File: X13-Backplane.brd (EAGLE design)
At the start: 86.4 x 139.3 mm, 36 parts, among them J1 PXC-PTSM-04-RA-1778641, J2 PXC-PTSM-04-RA-1778641, J3 PXC-8-RA-1778683, J4 PXC-PTSM-04-RA-1778641, J5 PXC-PTSM-04-RA-1778641, J6 284512-4, J8 PXC-8-RA-1778683

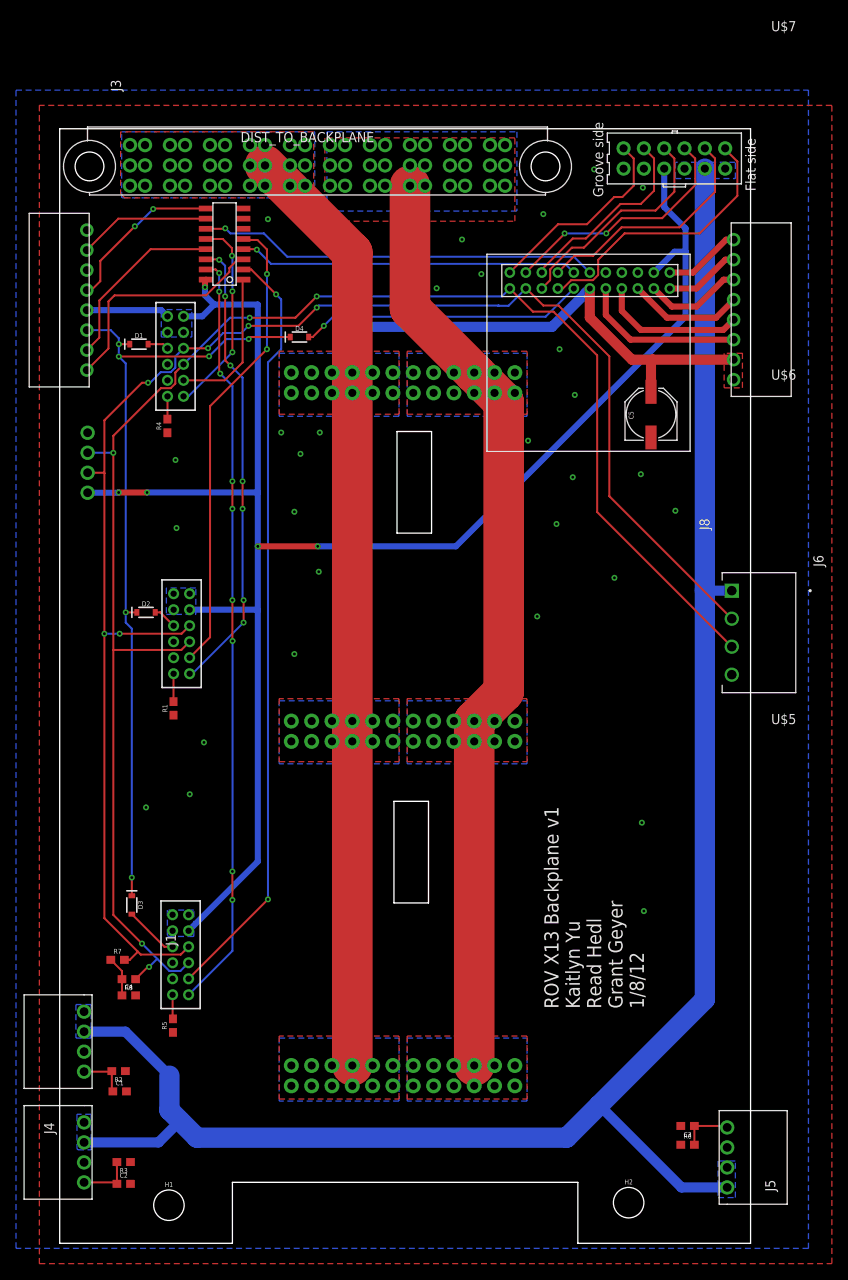
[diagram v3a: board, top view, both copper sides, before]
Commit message: Added third cutout and models for te 4 pin conn
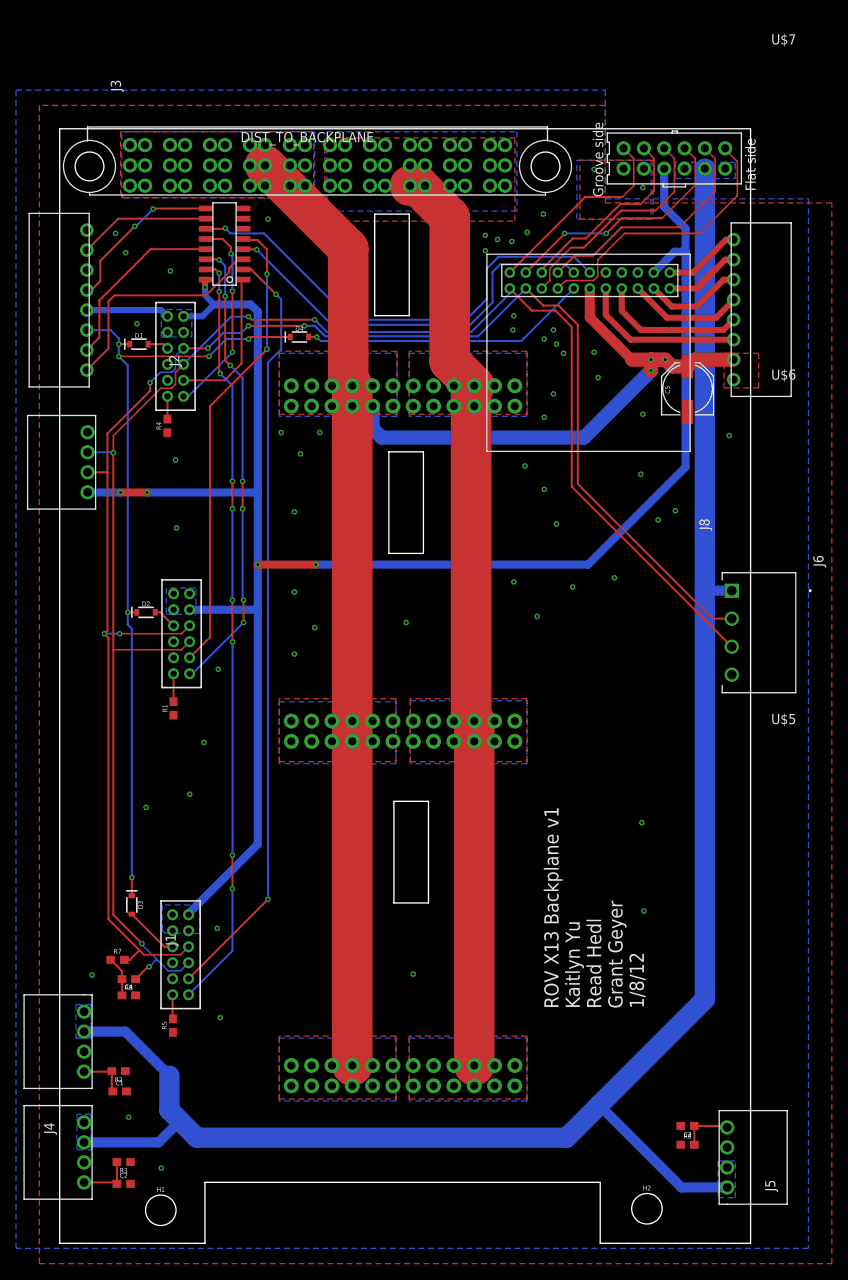
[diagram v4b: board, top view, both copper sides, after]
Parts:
- J6: value 284512-4 -> (none); device 284512-4:TE_284512-4 -> te 3.5m mm horiz 4 pin:TE_284512-4
- moved J2 7.56 mm to (11.1, 101.4), flipped to the top, turned to 270 degrees
- moved C5 5.57 mm to (86.1, 106.8)
- moved H2 2.41 mm to (81.0, 4.32)
- moved U$7 1.65 mm to (101.6, 143.5)
- moved H1 1.20 mm to (20.3, 4.13)
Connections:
- net 3.3V: now also J2.4; no longer J2.1
- net CAN_H: now also J2.3; no longer J2.2
- net CAN_L: now also J2.2; no longer J2.3
- net GND: now also J2.1; no longer J2.4
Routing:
- net 3.3V: track 225.7 -> 235.1 mm
- net SWCLK_4: track 50.3 -> 59.1 mm
- net SWDIO_4: track 42.5 -> 51.1 mm
- net 12V: track 181.8 -> 187.6 mm, vias 0 -> 3
- net CAN_H: track 203.8 -> 206.2 mm
- net CAN_L: track 205.3 -> 207.6 mm
- net 12VGND: track 116.4 -> 114.2 mm
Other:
- outline, holes or cut-outs redrawn

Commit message: add tStop polygon
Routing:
- net 12V: track 187.6 -> 209.1 mm
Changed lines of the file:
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@@
 <layer number="27" name="tValues" color="7" fill="1" visible="yes" active="yes"/>
 <layer number="28" name="bValues" color="7" fill="1" visible="yes" active="yes"/>
-<layer number="29" name="tStop" color="7" fill="3" visible="no" active="yes"/>
+<layer number="29" name="tStop" color="7" fill="3" visible="yes" active="yes"/>
 <layer number="30" name="bStop" color="7" fill="6" visible="no" active="yes"/>
 <layer number="31" name="tCream" color="7" fill="4" visible="no" active="yes"/>
@@
 <wire x1="51.308" y1="128.651" x2="51.308" y2="115.951" width="0" layer="20"/>
 <wire x1="51.308" y1="115.951" x2="46.99" y2="115.951" width="0" layer="20"/>
+<polygon width="0.1524" layer="29">
+<vertex x="41.529" y="17.526"/>
+<vertex x="46.736" y="17.526"/>
+<vertex x="46.736" y="112.014"/>
+<vertex x="46.355" y="112.014"/>
+<vertex x="46.355" y="125.222"/>
+<vertex x="41.148" y="130.429"/>
+<vertex x="33.655" y="130.429"/>
+<vertex x="40.64" y="123.444"/>
+<vertex x="40.64" y="103.632"/>
+<vertex x="41.529" y="102.743"/>
+</polygon>
+<polygon width="0.1524" layer="29">
+<vertex x="42.164" y="130.175"/>
+<vertex x="65.024" y="130.175"/>
+<vertex x="65.024" y="129.032"/>
+<vertex x="63.246" y="127.254"/>
+<vertex x="58.928" y="127.254"/>
+<vertex x="58.928" y="111.76"/>
+<vertex x="62.357" y="108.331"/>
+<vertex x="62.357" y="103.759"/>
+<vertex x="61.722" y="103.124"/>
+<vertex x="61.722" y="63.246"/>
+<vertex x="62.103" y="62.865"/>
+<vertex x="62.103" y="17.272"/>
+<vertex x="56.769" y="17.272"/>
+<vertex x="56.769" y="68.453"/>
+<vertex x="56.388" y="68.834"/>
+<vertex x="56.388" y="103.251"/>
+<vertex x="53.594" y="106.045"/>
+<vertex x="53.594" y="127.127"/>
+<vertex x="53.467" y="127.254"/>
+<vertex x="45.085" y="127.254"/>
+</polygon>
 </plain>
 <attributes>
@@
 <via x="70.612" y="111.252" extent="1-16" drill="0.35"/>
 <via x="74.93" y="108.204" extent="1-16" drill="0.35"/>
-<via x="74.422" y="111.379" extent="1-16" drill="0.35"/>
+<via x="75.438" y="110.236" extent="1-16" drill="0.35"/>
 <via x="68.199" y="103.251" extent="1-16" drill="0.35"/>
-<via x="80.518" y="103.632" extent="1-16" drill="0.35"/>
+<via x="81.534" y="102.235" extent="1-16" drill="0.35"/>
 <via x="91.313" y="100.965" extent="1-16" drill="0.35"/>
 <via x="16.256" y="15.748" extent="1-16" drill="0.35"/>
@@
 </polygon>
 <contactref element="J2" pad="1"/>
+<via x="39.37" y="72.263" extent="1-16" drill="0.35"/>
+<via x="30.607" y="58.42" extent="1-16" drill="0.35"/>
+<wire x1="30.57525" y1="126.8095" x2="21.463" y2="121.539" width="0" layer="19" extent="1-1"/>
 </signal>
 <signal name="SWDIO_3">
@@
 <wire x1="35.306" y1="117.983" x2="35.306" y2="111.76" width="0.254" layer="16"/>
 <wire x1="31.5595" y1="121.7295" x2="34.671" y2="118.618" width="0.254" layer="1"/>
-<wire x1="33.655" y1="42.99" x2="23.733" y2="33.068" width="0.254" layer="1"/>
+<wire x1="23.733" y1="33.068" x2="33.655" y2="42.99" width="0.254" layer="1"/>
 <wire x1="35.306" y1="111.76" x2="33.655" y2="110.109" width="0.254" layer="16"/>
 <wire x1="33.655" y1="110.109" x2="33.655" y2="42.99" width="0.254" layer="16"/>
@@
 <wire x1="29.21" y1="91.821" x2="29.21" y2="80.391" width="0.254" layer="16"/>
 <via x="29.21" y="80.391" extent="1-16" drill="0.35"/>
-<wire x1="29.21" y1="80.391" x2="29.21" y2="75.184" width="0.254" layer="1"/>
-<wire x1="29.21" y1="75.184" x2="29.23049375" y2="75.16350625" width="0.254" layer="1"/>
-<via x="29.23049375" y="75.16350625" extent="1-16" drill="0.35"/>
-<wire x1="29.23049375" y1="75.16350625" x2="29.23049375" y2="48.53449375" width="0.254" layer="16"/>
+<wire x1="29.21" y1="80.391" x2="29.21" y2="74.93" width="0.254" layer="1"/>
+<wire x1="29.21" y1="74.93" x2="29.23049375" y2="74.90950625" width="0.254" layer="1"/>
+<via x="29.23049375" y="74.90950625" extent="1-16" drill="0.35"/>
+<wire x1="29.23049375" y1="74.90950625" x2="29.23049375" y2="48.53449375" width="0.254" layer="16"/>
 <wire x1="29.23049375" y1="48.53449375" x2="29.21" y2="48.514" width="0.254" layer="16"/>
 <via x="29.21" y="48.514" extent="1-16" drill="0.35"/>
@@
 <wire x1="39.624" y1="84.836" x2="32.385" y2="84.836" width="1.016" layer="1"/>
 <via x="32.385" y="84.836" extent="1-16" drill="0.35"/>
-<wire x1="73.66" y1="84.836" x2="85.852" y2="97.028" width="1.016" layer="16"/>
+<wire x1="85.852" y1="97.028" x2="73.66" y2="84.836" width="1.016" layer="16"/>
 <wire x1="85.852" y1="97.028" x2="85.852" y2="123.952" width="1.016" layer="16"/>
-<wire x1="39.624" y1="84.836" x2="73.66" y2="84.836" width="1.016" layer="16"/>
+<wire x1="73.66" y1="84.836" x2="39.624" y2="84.836" width="1.016" layer="16"/>
 <wire x1="32.385" y1="49.879" x2="23.733" y2="41.227" width="1.016" layer="16"/>
 <wire x1="23.733" y1="41.068" x2="23.733" y2="41.227" width="0.762" layer="16"/>
@@
 <wire x1="65.9445" y1="119.3485" x2="68.072" y2="117.221" width="0.254" layer="1"/>
 <wire x1="68.072" y1="117.221" x2="69.977" y2="117.221" width="0.254" layer="1"/>
-<wire x1="69.977" y1="117.221" x2="72.39" y2="114.808" width="0.254" layer="1"/>
-<wire x1="72.39" y1="114.808" x2="72.39" y2="94.9045" width="0.254" layer="1"/>
-<wire x1="89.2175" y1="78.077" x2="91.6305" y2="78.077" width="0.254" layer="1"/>
-<wire x1="89.2175" y1="78.077" x2="72.39" y2="94.9045" width="0.254" layer="1"/>
+<wire x1="69.977" y1="117.221" x2="73.152" y2="114.046" width="0.254" layer="1"/>
+<wire x1="73.152" y1="114.046" x2="73.152" y2="94.0155" width="0.254" layer="1"/>
+<wire x1="89.0905" y1="78.077" x2="91.6305" y2="78.077" width="0.254" layer="1"/>
+<wire x1="89.0905" y1="78.077" x2="73.152" y2="94.0155" width="0.254" layer="1"/>
 <contactref element="J2" pad="3"/>
 <wire x1="11.1125" y1="96.37775" x2="13.57375" y2="96.37775" width="0.254" layer="1"/>
@@
 <wire x1="63.8835" y1="119.3485" x2="66.646" y2="116.586" width="0.254" layer="1"/>
 <wire x1="66.646" y1="116.586" x2="69.596" y2="116.586" width="0.254" layer="1"/>
-<wire x1="69.596" y1="116.586" x2="71.628" y2="114.554" width="0.254" layer="1"/>
-<wire x1="71.628" y1="114.554" x2="71.628" y2="94.5795" width="0.254" layer="1"/>
-<wire x1="71.628" y1="94.5795" x2="91.6305" y2="74.577" width="0.254" layer="1"/>
+<wire x1="69.596" y1="116.586" x2="72.517" y2="113.665" width="0.254" layer="1"/>
+<wire x1="72.517" y1="113.665" x2="72.517" y2="93.6905" width="0.254" layer="1"/>
+<wire x1="72.517" y1="93.6905" x2="91.6305" y2="74.577" width="0.254" layer="1"/>
 <wire x1="14.3256" y1="98.806" x2="14.3256" y2="74.168" width="0.254" layer="1"/>
 <wire x1="14.351" y1="74.1934" x2="14.3256" y2="74.168" width="0.2032" layer="1"/>
@@
 <vertex x="39.37" y="138.938"/>
 </polygon>
-<polygon width="0.762" layer="16">
+<polygon width="0.762" layer="16" isolate="0.508">
 <vertex x="39.497" y="138.938"/>
 <vertex x="39.497" y="131.191"/>
-<vertex x="38.989" y="130.683"/>
-<vertex x="15.367" y="130.683"/>
-<vertex x="15.367" y="138.938"/>
+<vertex x="37.338" y="129.032"/>
+<vertex x="13.081" y="129.032"/>
+<vertex x="13.081" y="138.938"/>
 </polygon>
 <polygon width="0.762" layer="1">
@@
 <wire x1="46.736" y1="104.648" x2="46.736" y2="101.854" width="1.778" layer="16"/>
 <wire x1="46.736" y1="101.854" x2="47.879" y2="100.711" width="1.778" layer="16"/>
-<wire x1="73.152" y1="100.711" x2="81.534" y2="109.093" width="1.778" layer="16"/>
+<wire x1="81.534" y1="106.807" x2="81.534" y2="109.093" width="1.778" layer="16"/>
+<wire x1="81.534" y1="106.807" x2="75.438" y2="100.711" width="1.778" layer="16"/>
 <via x="81.534" y="109.093" extent="1-16" drill="0.35"/>
-<wire x1="47.879" y1="100.711" x2="73.152" y2="100.711" width="1.778" layer="16"/>
+<wire x1="47.879" y1="100.711" x2="75.438" y2="100.711" width="1.778" layer="16"/>
 <wire x1="81.534" y1="109.093" x2="81.534" y2="110.4545" width="1.778" layer="16"/>
 <via x="81.534" y="110.4545" extent="1-16" drill="0.35"/>
@@
 <wire x1="81.534" y1="110.4545" x2="79.15335" y2="110.4545" width="1.778" layer="1"/>
 <wire x1="81.534" y1="109.093" x2="81.534" y2="110.4545" width="1.778" layer="1"/>
+<wire x1="18.28625" y1="132.20125" x2="18.415" y2="132.0725" width="0.508" layer="1"/>
+<wire x1="18.415" y1="132.0725" x2="18.415" y2="130.683" width="0.508" layer="1"/>
+<wire x1="16.40625" y1="132.20125" x2="16.40625" y2="130.91375" width="0.508" layer="1"/>
+<wire x1="16.40625" y1="130.91375" x2="16.637" y2="130.683" width="0.508" layer="1"/>
+<wire x1="16.637" y1="130.683" x2="18.415" y2="130.683" width="0.508" layer="1"/>
+<wire x1="18.415" y1="130.683" x2="33.655" y2="130.683" width="0.508" layer="1"/>
 </signal>
 <signal name="SWCLK_IN">
@@
 <contactref element="DIST_TO_BACKPLANE" pad="4@6"/>
 <contactref element="DIST_TO_BACKPLANE" pad="4@1"/>
-<polygon width="0.762" layer="1">
+<polygon width="0.762" layer="1" isolate="0.508">
 <vertex x="40.767" y="138.176"/>
 <vertex x="40.767" y="127.762"/>
-<vertex x="64.516" y="127.762"/>
+<vertex x="63.119" y="127.762"/>
+<vertex x="64.516" y="129.159"/>
 <vertex x="64.516" y="138.176"/>
 </polygon>
